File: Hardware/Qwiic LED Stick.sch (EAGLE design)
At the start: 46 parts, among them J2 QWIIC_RA, J4 QWIIC_RA, J6 AVR_SPI_PROG_3X2TESTPOINTS, U2 ATTINY85

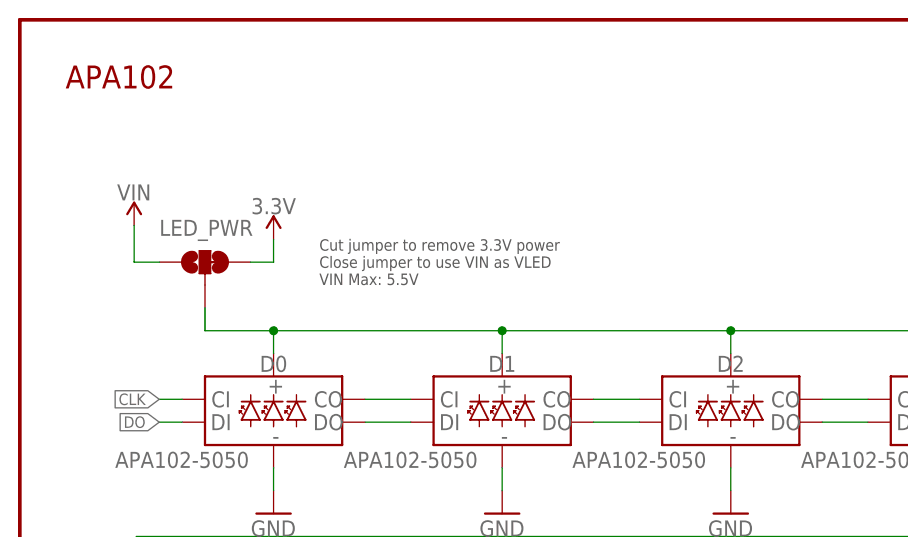
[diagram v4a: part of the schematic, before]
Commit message: Update comments on sch
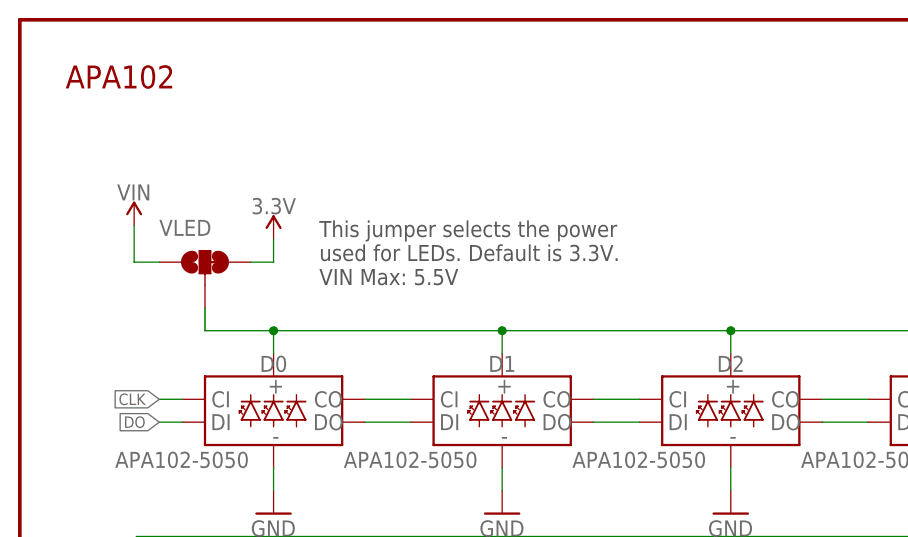
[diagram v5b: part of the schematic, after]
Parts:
- renumbered LED_PWR to VLED
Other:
- note added: "This jumper selects the power used for LEDs. Default is 3.3V. VIN Max: 5.5V"
- note removed: "Cut jumper to remove 3.3V power Close jumper to use VIN as VLED VIN Max: 5.5V"
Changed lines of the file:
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@@
 <part name="GND9" library="SparkFun-PowerSymbols" deviceset="GND" device=""/>
 <part name="ADDR" library="SparkFun-Jumpers" deviceset="JUMPER-SMT_2_NO" device="_SILK" package3d_urn="urn:adsk.eagle:package:39279/1"/>
-<part name="LED_PWR" library="SparkFun-Jumpers" deviceset="JUMPER-SMT_3_1-NC_TRACE" device="_SILK" package3d_urn="urn:adsk.eagle:package:39288/1" value="JUMPER-SMT_3_1-NC_TRACE_SILK"/>
+<part name="VLED" library="SparkFun-Jumpers" deviceset="JUMPER-SMT_3_1-NC_TRACE" device="_SILK" package3d_urn="urn:adsk.eagle:package:39288/1" value="JUMPER-SMT_3_1-NC_TRACE_SILK"/>
 <part name="J1" library="SparkFun-Connectors" deviceset="CONN_02" device="1X02_NO_SILK"/>
 <part name="J5" library="SparkFun-Connectors" deviceset="CONN_04" device="1X04_NO_SILK"/>
@@
 Closed Jumper: 0x22</text>
 <wire x1="0" y1="88.9" x2="160.02" y2="88.9" width="0.2032" layer="97" style="longdash"/>
-<text x="33.274" y="155.956" size="1.27" layer="97" font="vector">Cut jumper to remove 3.3V power
-Close jumper to use VIN as VLED
+<text x="33.274" y="155.956" size="1.778" layer="97" font="vector">This jumper selects the power
+used for LEDs. Default is 3.3V.
 VIN Max: 5.5V</text>
 <text x="148.59" y="6.604" size="2.54" layer="94" font="vector">Revised by: Priyanka Makin</text>
@@
 <attribute name="NAME" x="130.048" y="54.864" size="1.778" layer="95" font="vector" rot="R90"/>
 </instance>
-<instance part="LED_PWR" gate="G$1" x="20.574" y="158.496" smashed="yes" rot="R90">
+<instance part="VLED" gate="G$1" x="20.574" y="158.496" smashed="yes" rot="R90">
 <attribute name="NAME" x="15.494" y="161.417" size="1.778" layer="95" font="vector"/>
 </instance>
@@
 </segment>
 <segment>
-<pinref part="LED_PWR" gate="G$1" pin="3"/>
+<pinref part="VLED" gate="G$1" pin="3"/>
 <wire x1="25.654" y1="158.496" x2="28.194" y2="158.496" width="0.1524" layer="91"/>
 <pinref part="SUPPLY18" gate="G$1" pin="3.3V"/>
@@
 <wire x1="28.194" y1="150.876" x2="20.574" y2="150.876" width="0.1524" layer="91"/>
 <junction x="28.194" y="150.876"/>
-<pinref part="LED_PWR" gate="G$1" pin="2"/>
+<pinref part="VLED" gate="G$1" pin="2"/>
 <wire x1="20.574" y1="150.876" x2="20.574" y2="153.416" width="0.1524" layer="91"/>
 <junction x="104.394" y="150.876"/>
@@
 </segment>
 <segment>
-<pinref part="LED_PWR" gate="G$1" pin="1"/>
+<pinref part="VLED" gate="G$1" pin="1"/>
 <pinref part="SUPPLY2" gate="G$1" pin="VIN"/>
 <wire x1="15.494" y1="158.496" x2="12.7" y2="158.496" width="0.1524" layer="91"/>
